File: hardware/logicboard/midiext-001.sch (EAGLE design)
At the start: 19 parts, among them IC1 74LS07N, IC2 LTC485N, IC3 LTC485N, X1 JST-2PINPH

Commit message: New schematic.
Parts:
- removed C6: 103, rcl:C-US025-025X050
- removed D2: BAS15, diode:BAS15
- removed J5, J6: (no value), SparkFun-Connectors:CONN_04X2
- removed R10, R6, R7: 220, resistor:R-US_0204/5
- removed R8, R9: 120, resistor:R-US_0204/5
- removed X1: JST-2PINPH, con-jst:JST-2PINPH
- added CN1, CN3, CN4: (no value), adafruit:JST_2PIN-SMT-RA
- added CN2, CN5: (no value), adafruit:JST_3PIN
- added D1: BAS15, diode:BAS15
- added R1, R2, R3: 220, resistor:R-US_0204/5
- added R4, R5: 120, resistor:R-US_0204/5
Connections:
- removed net COM3: IC2.DI
- removed net COM4: IC3.RO
- removed net COM5: J6.8
- removed net VDD: X1.1
- net COM1: now also IC2.RO
- net COM2: now also IC3.DI
- net GND: now also CN1.1, CN2.2, CN5.2, IC2.!RE, IC2.DE, IC2.DI; no longer C6.2, IC3.!RE, IC3.DE, IC3.DI, J5.2, J6.2, X1.2
- net MIDIRX+: now also CN3.2, R3.2; no longer J6.4, R6.2
- net MIDIRX-: now also CN3.1, D1.A; no longer D2.A, J6.5
- net MIDITX+: now also CN2.1, R2.1; no longer J5.4, R10.2
- net MIDITX-: now also CN2.3, R1.2; no longer J5.5, R7.2
- net N$15: now also D1.C, R3.1; no longer D2.C, R6.1
- net N$2: now also R1.1; no longer R7.1
- net RX+: now also CN4.2, IC2.A, R4.2; no longer IC3.A, J6.6, R9.2
- net RX-: now also CN4.1, IC2.B, R4.1; no longer IC3.B, J6.7, R9.1
- net TX+: now also CN5.1, IC3.A, R5.2; no longer IC2.A, J5.6, R8.2
- net TX-: now also CN5.3, IC3.B, R5.1; no longer IC2.B, J5.7, R8.1
- net VCC: now also CN1.2, IC3.!RE, IC3.DE, R2.2; no longer C6.1, IC2.!RE, IC2.DE, R10.1
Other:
- moved on the sheet: C1, C2, C3, C4, C5, IC1A, IC1B, IC1C, IC1D, IC1E, IC1F, IC2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

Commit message: Changed connectors.
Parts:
- removed CN1, CN3, CN4: (no value), adafruit:JST_2PIN-SMT-RA
- removed CN2, CN5: (no value), adafruit:JST_3PIN
- added J1, J2, J3: (no value), SparkFun-Connectors:CONN_02JST-PTH-2
- added J4, J5: (no value), SparkFun-Connectors:CONN_03JST-PTH
- added J6: (no value), SparkFun-Connectors:CONN_04JST-PTH
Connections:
- net GND: now also J1.2, J4.2, J5.2; no longer CN1.1, CN2.2, CN5.2
- net MIDIRX+: now also J2.1; no longer CN3.2
- net MIDIRX-: now also J2.2; no longer CN3.1
- net MIDITX+: now also J4.1; no longer CN2.1
- net MIDITX-: now also J4.3; no longer CN2.3
- net RX+: now also J3.1; no longer CN4.2
- net RX-: now also J3.2; no longer CN4.1
- net TX+: now also J5.1; no longer CN5.1
- net TX-: now also J5.3; no longer CN5.3
- net VCC: now also J1.1; no longer CN1.2
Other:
- moved on the sheet: IC2, R4

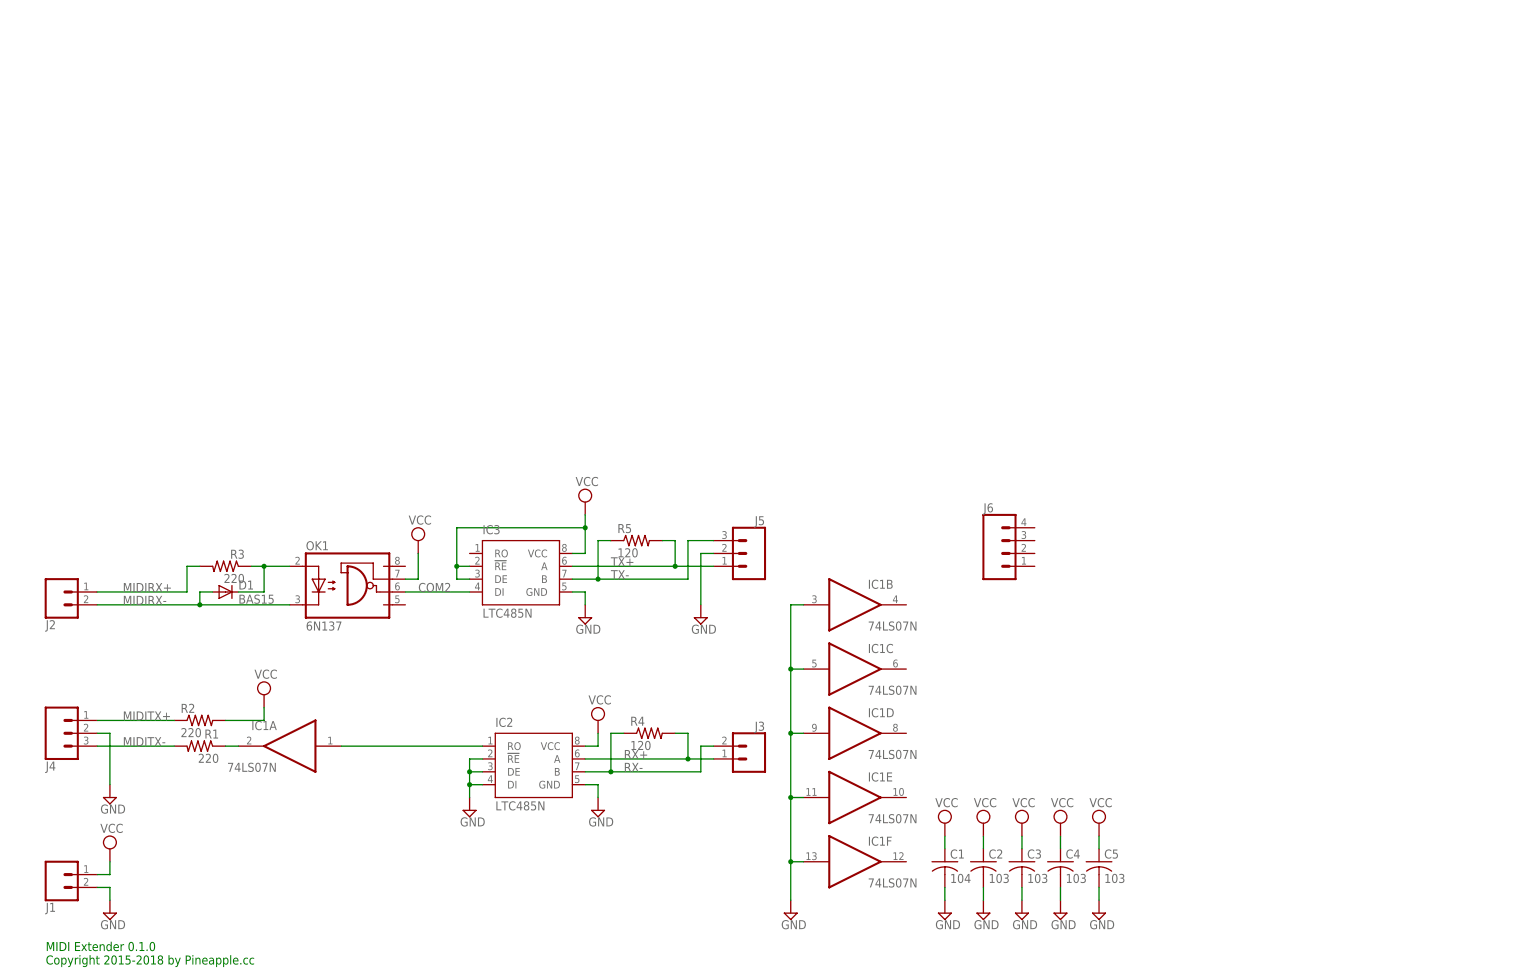
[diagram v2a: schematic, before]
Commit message: Now has LED indicator port.
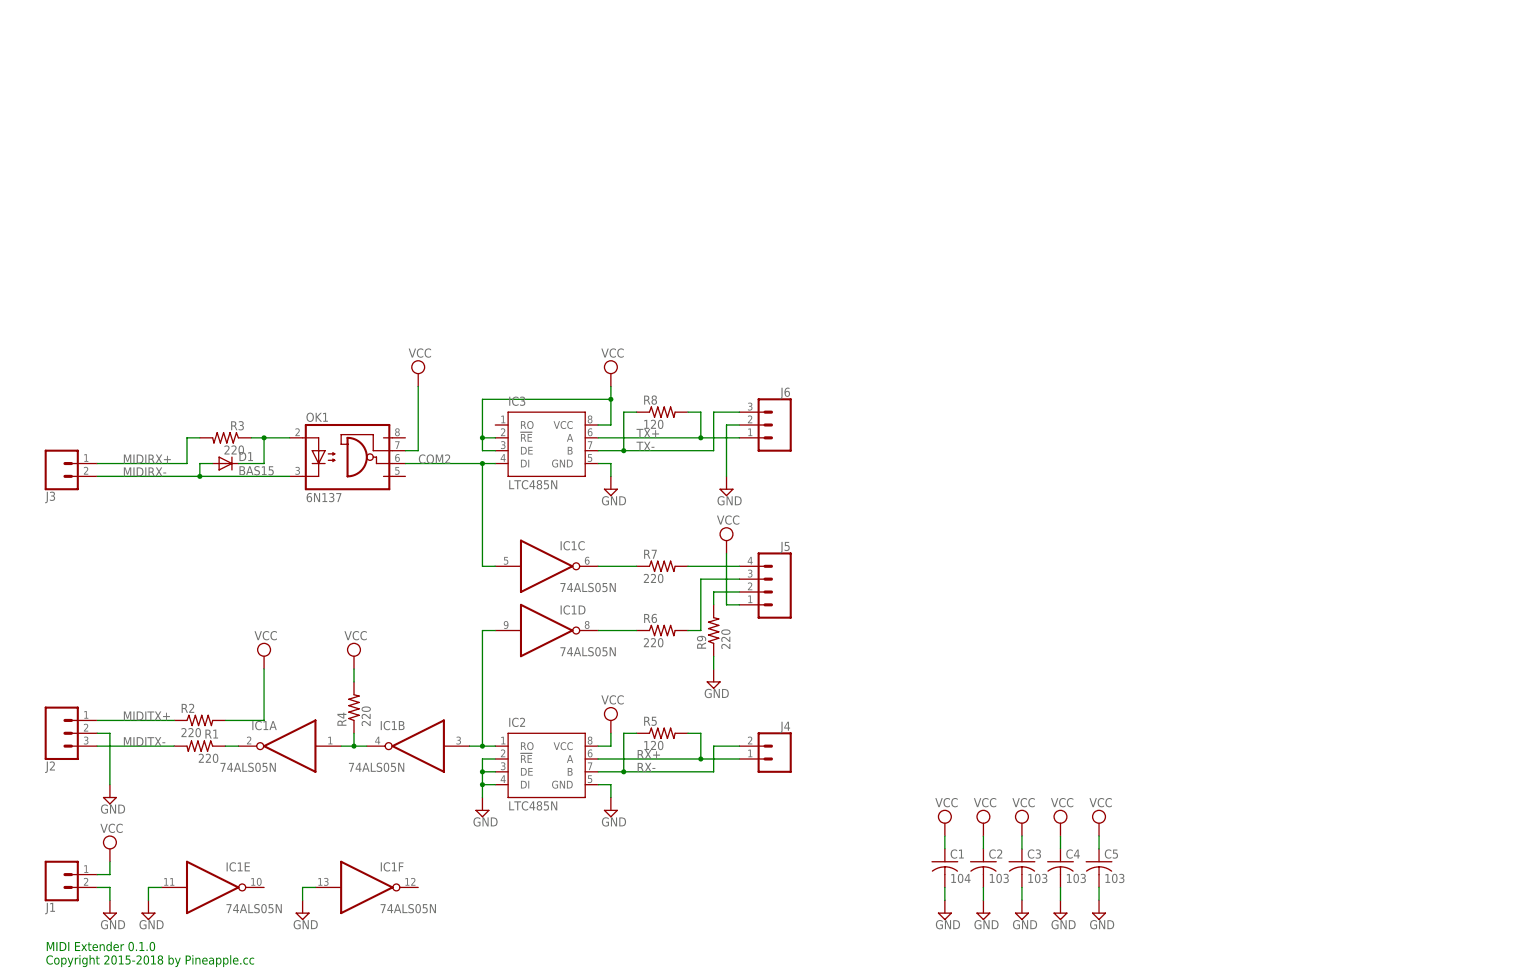
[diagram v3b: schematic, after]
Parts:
- added R6, R7, R9: 220, resistor:R-US_0204/5
- added R8: 120, resistor:R-US_0204/5
- IC1: value 74LS07N -> 74ALS05N; device 74xx-us:74LS07N -> 74xx-eu:74ALS05N
- J2: device SparkFun-Connectors:CONN_02JST-PTH-2 -> SparkFun-Connectors:CONN_03JST-PTH
- J4: device SparkFun-Connectors:CONN_03JST-PTH -> SparkFun-Connectors:CONN_02JST-PTH-2
- J5: device SparkFun-Connectors:CONN_03JST-PTH -> SparkFun-Connectors:CONN_04JST-PTH
- J6: device SparkFun-Connectors:CONN_04JST-PTH -> SparkFun-Connectors:CONN_03JST-PTH
- R4: value 120 -> 220
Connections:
- removed net COM1: IC1A.I, IC2.RO
- new net N$1: IC1B.I, IC1D.I, IC2.RO
- new net N$10: J5.2, R9.2
- new net N$3: IC1A.I, IC1B.O, R4.1
- new net N$6: IC1C.O, R7.1
- new net N$7: IC1D.O, R6.1
- new net N$8: J5.4, R7.2
- new net N$9: J5.3, R6.2
- net COM2: now also IC1C.I
- net GND: now also J2.2, J6.2, R9.1; no longer IC1B.I, IC1C.I, IC1D.I, J4.2, J5.2
- net MIDIRX+: now also J3.1; no longer J2.1
- net MIDIRX-: now also J3.2; no longer J2.2
- net MIDITX+: now also J2.1; no longer J4.1
- net MIDITX-: now also J2.3; no longer J4.3
- net RX+: now also J4.1, R5.2; no longer J3.1, R4.2
- net RX-: now also J4.2, R5.1; no longer J3.2, R4.1
- net TX+: now also J6.1, R8.2; no longer J5.1, R5.2
- net TX-: now also J6.3, R8.1; no longer J5.3, R5.1
- net VCC: now also J5.1, R4.2
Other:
- moved on the sheet: D1, IC2, IC3, J3, OK1, R3, R4, R5

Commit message: Now has LED indicator panel.
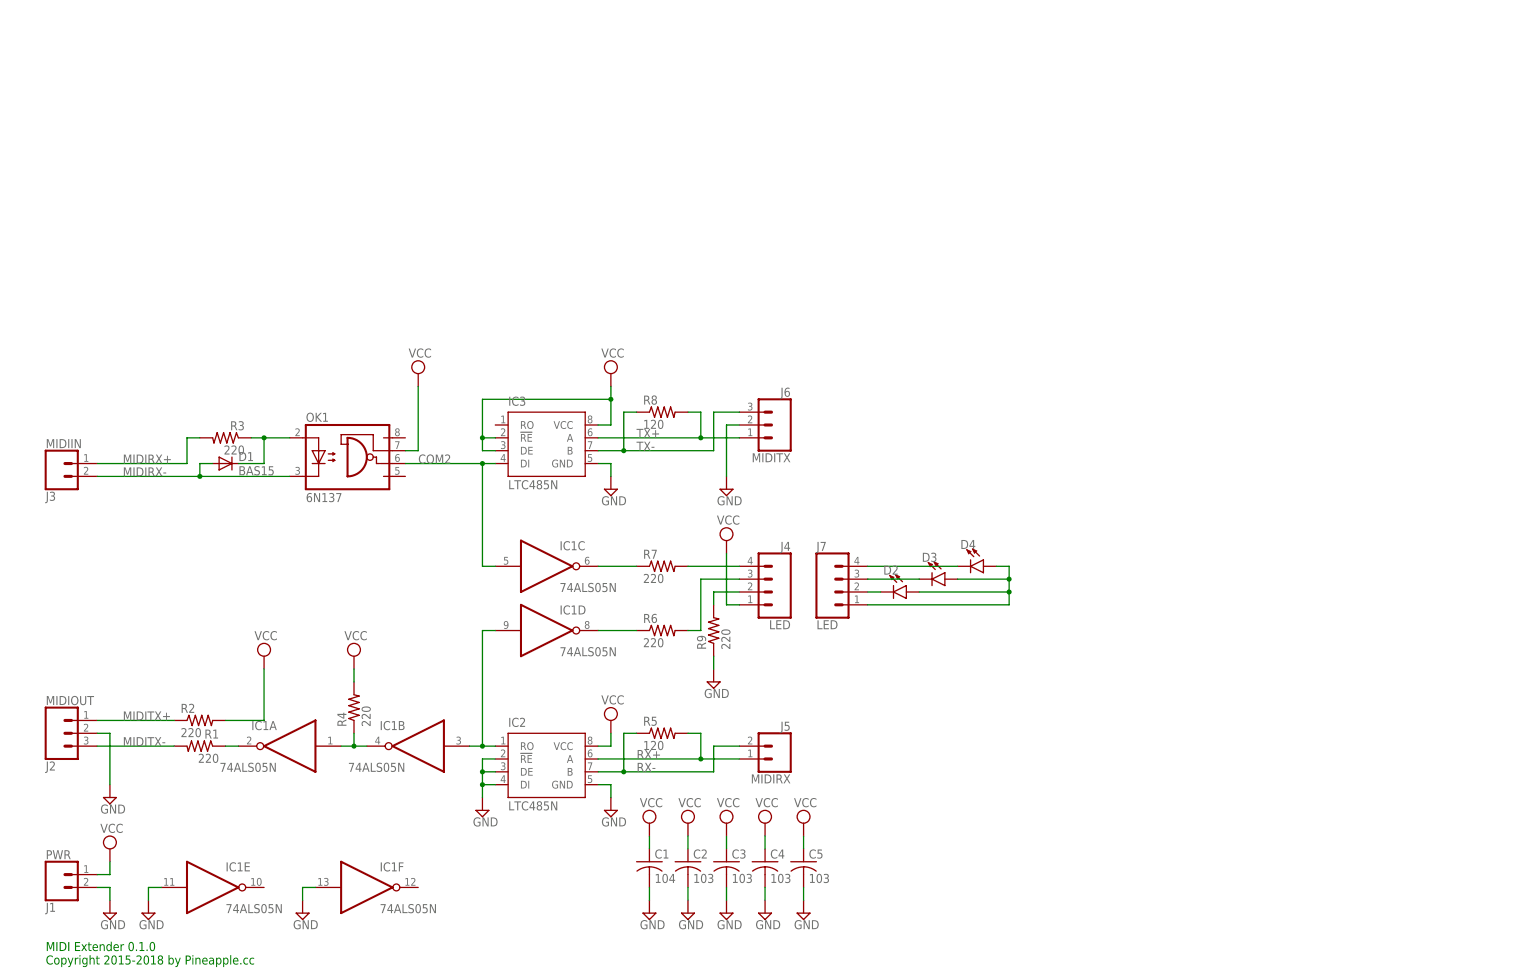
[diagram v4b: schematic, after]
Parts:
- added D2, D3, D4: (no value), SparkFun-LED:LED3MM
- added J7: LED, SparkFun-Connectors:CONN_04JST-PTH
- J1: value (none) -> PWR
- J2: value (none) -> MIDIOUT
- J3: value (none) -> MIDIIN
- J4: value (none) -> LED; device SparkFun-Connectors:CONN_02JST-PTH-2 -> SparkFun-Connectors:CONN_04JST-PTH
- J5: value (none) -> MIDIRX; device SparkFun-Connectors:CONN_04JST-PTH -> SparkFun-Connectors:CONN_02JST-PTH-2
- J6: value (none) -> MIDITX
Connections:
- new net N$11: D3.C, J7.3
- new net N$12: D4.C, J7.4
- new net N$4: D2.A, D3.A, D4.A, J7.1
- new net N$5: D2.C, J7.2
- net N$10: now also J4.2; no longer J5.2
- net N$8: now also J4.4; no longer J5.4
- net N$9: now also J4.3; no longer J5.3
- net RX+: now also J5.1; no longer J4.1
- net RX-: now also J5.2; no longer J4.2
- net VCC: now also J4.1; no longer J5.1
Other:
- moved on the sheet: C1, C2, C3, C4, C5

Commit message: First try.
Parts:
- D2: value (none) -> PWR
- D3: value (none) -> OUT
- D4: value (none) -> IN
- J7: device SparkFun-Connectors:CONN_04JST-PTH -> SparkFun-Connectors:CONN_04JST-PTH-VERT
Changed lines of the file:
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@@
 <?xml version="1.0" encoding="utf-8"?>
 <!DOCTYPE eagle SYSTEM "eagle.dtd">
-<eagle version="8.6.2">
+<eagle version="8.6.3">
 <drawing>
 <settings>
@@
 <setting verticaltext="up"/>
 </settings>
-<grid distance="0.1" unitdist="inch" unit="inch" style="lines" multiple="1" display="yes" altdistance="0.01" altunitdist="inch" altunit="inch"/>
+<grid distance="0.1" unitdist="inch" unit="inch" style="lines" multiple="1" display="no" altdistance="0.01" altunitdist="inch" altunit="inch"/>
 <layers>
 <layer number="1" name="Top" color="4" fill="1" visible="no" active="no"/>
@@
 <part name="SUPPLY18" library="supply2" library_urn="urn:adsk.eagle:library:372" deviceset="GND" device=""/>
 <part name="SUPPLY21" library="supply2" library_urn="urn:adsk.eagle:library:372" deviceset="VCC" device=""/>
-<part name="J7" library="SparkFun-Connectors" deviceset="CONN_04" device="JST-PTH" value="LED"/>
-<part name="D2" library="SparkFun-LED" deviceset="LED" device="3MM"/>
-<part name="D3" library="SparkFun-LED" deviceset="LED" device="3MM"/>
-<part name="D4" library="SparkFun-LED" deviceset="LED" device="3MM"/>
+<part name="J7" library="SparkFun-Connectors" deviceset="CONN_04" device="JST-PTH-VERT" value="LED"/>
+<part name="D2" library="SparkFun-LED" deviceset="LED" device="3MM" value="PWR"/>
+<part name="D3" library="SparkFun-LED" deviceset="LED" device="3MM" value="OUT"/>
+<part name="D4" library="SparkFun-LED" deviceset="LED" device="3MM" value="IN"/>
 </parts>
 <sheets>

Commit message: Removed LED panel from main logic board.
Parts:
- removed D2: PWR, SparkFun-LED:LED3MM
- removed D3: OUT, SparkFun-LED:LED3MM
- removed D4: IN, SparkFun-LED:LED3MM
- removed J7: LED, SparkFun-Connectors:CONN_04JST-PTH-VERT
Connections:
- removed net N$11: D3.C, J7.3
- removed net N$12: D4.C, J7.4
- removed net N$4: D2.A, D3.A, D4.A, J7.1
- removed net N$5: D2.C, J7.2
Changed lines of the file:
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@@
 <part name="SUPPLY18" library="supply2" library_urn="urn:adsk.eagle:library:372" deviceset="GND" device=""/>
 <part name="SUPPLY21" library="supply2" library_urn="urn:adsk.eagle:library:372" deviceset="VCC" device=""/>
-<part name="J7" library="SparkFun-Connectors" deviceset="CONN_04" device="JST-PTH-VERT" value="LED"/>
-<part name="D2" library="SparkFun-LED" deviceset="LED" device="3MM" value="PWR"/>
-<part name="D3" library="SparkFun-LED" deviceset="LED" device="3MM" value="OUT"/>
-<part name="D4" library="SparkFun-LED" deviceset="LED" device="3MM" value="IN"/>
 </parts>
 <sheets>
@@
 <instance part="SUPPLY18" gate="GND" x="134.62" y="58.42"/>
 <instance part="SUPPLY21" gate="G$1" x="137.16" y="86.36"/>
-<instance part="J7" gate="G$1" x="160.02" y="76.2"/>
-<instance part="D2" gate="G$1" x="172.72" y="76.2" rot="R270"/>
-<instance part="D3" gate="G$1" x="180.34" y="78.74" rot="R270"/>
-<instance part="D4" gate="G$1" x="187.96" y="81.28" rot="R270"/>
 </instances>
 <busses>
@@
 </segment>
 </net>
-<net name="N$4" class="0">
-<segment>
-<pinref part="J7" gate="G$1" pin="1"/>
-<wire x1="165.1" y1="73.66" x2="193.04" y2="73.66" width="0.1524" layer="91"/>
-<wire x1="193.04" y1="73.66" x2="193.04" y2="76.2" width="0.1524" layer="91"/>
-<pinref part="D4" gate="G$1" pin="A"/>
-<wire x1="193.04" y1="76.2" x2="193.04" y2="78.74" width="0.1524" layer="91"/>
-<wire x1="193.04" y1="78.74" x2="193.04" y2="81.28" width="0.1524" layer="91"/>
-<wire x1="193.04" y1="81.28" x2="190.5" y2="81.28" width="0.1524" layer="91"/>
-<pinref part="D3" gate="G$1" pin="A"/>
-<wire x1="182.88" y1="78.74" x2="193.04" y2="78.74" width="0.1524" layer="91"/>
-<junction x="193.04" y="78.74"/>
-<pinref part="D2" gate="G$1" pin="A"/>
-<wire x1="175.26" y1="76.2" x2="193.04" y2="76.2" width="0.1524" layer="91"/>
-<junction x="193.04" y="76.2"/>
-</segment>
-</net>
-<net name="N$5" class="0">
-<segment>
-<pinref part="J7" gate="G$1" pin="2"/>
-<pinref part="D2" gate="G$1" pin="C"/>
-<wire x1="167.64" y1="76.2" x2="165.1" y2="76.2" width="0.1524" layer="91"/>
-</segment>
-</net>
-<net name="N$11" class="0">
-<segment>
-<pinref part="J7" gate="G$1" pin="3"/>
-<pinref part="D3" gate="G$1" pin="C"/>
-<wire x1="175.26" y1="78.74" x2="165.1" y2="78.74" width="0.1524" layer="91"/>
-</segment>
-</net>
-<net name="N$12" class="0">
-<segment>
-<pinref part="J7" gate="G$1" pin="4"/>
-<pinref part="D4" gate="G$1" pin="C"/>
-<wire x1="182.88" y1="81.28" x2="165.1" y2="81.28" width="0.1524" layer="91"/>
-</segment>
-</net>

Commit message: Fixed values.
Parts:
- R6, R7, R9: value 220 -> 330
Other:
- note added: "MIDI Extender 1.0.0 Copyright 2015-2018 by Pineapple.cc"
- note removed: "MIDI Extender 0.1.0 Copyright 2015-2018 by Pineapple.cc"
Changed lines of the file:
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@@
 <part name="SUPPLY7" library="supply2" library_urn="urn:adsk.eagle:library:372" deviceset="VCC" device=""/>
 <part name="SUPPLY4" library="supply2" library_urn="urn:adsk.eagle:library:372" deviceset="GND" device=""/>
-<part name="R7" library="resistor" library_urn="urn:adsk.eagle:library:348" deviceset="R-US_" device="0204/5" package3d_urn="urn:adsk.eagle:package:25955/1" value="220"/>
-<part name="R6" library="resistor" library_urn="urn:adsk.eagle:library:348" deviceset="R-US_" device="0204/5" package3d_urn="urn:adsk.eagle:package:25955/1" value="220"/>
-<part name="R9" library="resistor" library_urn="urn:adsk.eagle:library:348" deviceset="R-US_" device="0204/5" package3d_urn="urn:adsk.eagle:package:25955/1" value="220"/>
+<part name="R7" library="resistor" library_urn="urn:adsk.eagle:library:348" deviceset="R-US_" device="0204/5" package3d_urn="urn:adsk.eagle:package:25955/1" value="330"/>
+<part name="R6" library="resistor" library_urn="urn:adsk.eagle:library:348" deviceset="R-US_" device="0204/5" package3d_urn="urn:adsk.eagle:package:25955/1" value="330"/>
+<part name="R9" library="resistor" library_urn="urn:adsk.eagle:library:348" deviceset="R-US_" device="0204/5" package3d_urn="urn:adsk.eagle:package:25955/1" value="330"/>
 <part name="SUPPLY18" library="supply2" library_urn="urn:adsk.eagle:library:372" deviceset="GND" device=""/>
 <part name="SUPPLY21" library="supply2" library_urn="urn:adsk.eagle:library:372" deviceset="VCC" device=""/>
@@
 <sheet>
 <plain>
-<text x="2.54" y="2.54" size="1.778" layer="91">MIDI Extender 0.1.0
+<text x="2.54" y="2.54" size="1.778" layer="91">MIDI Extender 1.0.0
 Copyright 2015-2018 by Pineapple.cc</text>
 </plain>

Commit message: Renumbered components.
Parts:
- J1: value PWR -> MIDIIN
- J3: value MIDIIN -> PWR
- J5: value MIDIRX -> MIDITX; device SparkFun-Connectors:CONN_02JST-PTH-2 -> SparkFun-Connectors:CONN_03JST-PTH
- J6: value MIDITX -> MIDIRX; device SparkFun-Connectors:CONN_03JST-PTH -> SparkFun-Connectors:CONN_02JST-PTH-2
- R4: value 220 -> 10k
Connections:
- net COM2: now also IC2.DI; no longer IC3.DI
- net GND: now also IC3.!RE, IC3.DE, IC3.DI, J3.2, J5.2; no longer IC2.!RE, IC2.DE, IC2.DI, J1.2, J6.2
- net MIDIRX+: now also J1.1; no longer J3.1
- net MIDIRX-: now also J1.2; no longer J3.2
- net MIDITX+: now also R1.1; no longer R2.1
- net MIDITX-: now also R2.2; no longer R1.2
- net N$1: now also IC3.RO; no longer IC2.RO
- net N$2: now also R2.1; no longer R1.1
- net N$6: now also R6.1; no longer R7.1
- net N$7: now also R7.1; no longer R6.1
- net N$8: now also R6.2; no longer R7.2
- net N$9: now also R7.2; no longer R6.2
- net RX+: now also IC3.A, J6.1, R8.2; no longer IC2.A, J5.1, R5.2
- net RX-: now also IC3.B, J6.2, R8.1; no longer IC2.B, J5.2, R5.1
- net TX+: now also IC2.A, J5.1, R5.2; no longer IC3.A, J6.1, R8.2
- net TX-: now also IC2.B, J5.3, R5.1; no longer IC3.B, J6.3, R8.1
- net VCC: now also IC2.!RE, IC2.DE, J3.1, R1.2; no longer IC3.!RE, IC3.DE, J1.1, R2.2
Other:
- moved on the sheet: IC2, IC3, J1, J3, R1, R2, R5, R6, R7, R8
